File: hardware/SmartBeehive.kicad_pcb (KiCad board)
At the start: 4 copper layers, 7 parts, among them U1 ESP32-S3-DevKitC, U2 HX711_Module, U3 SSD1306, U4 DS18B20, U5 INMP441, U6 SHT31

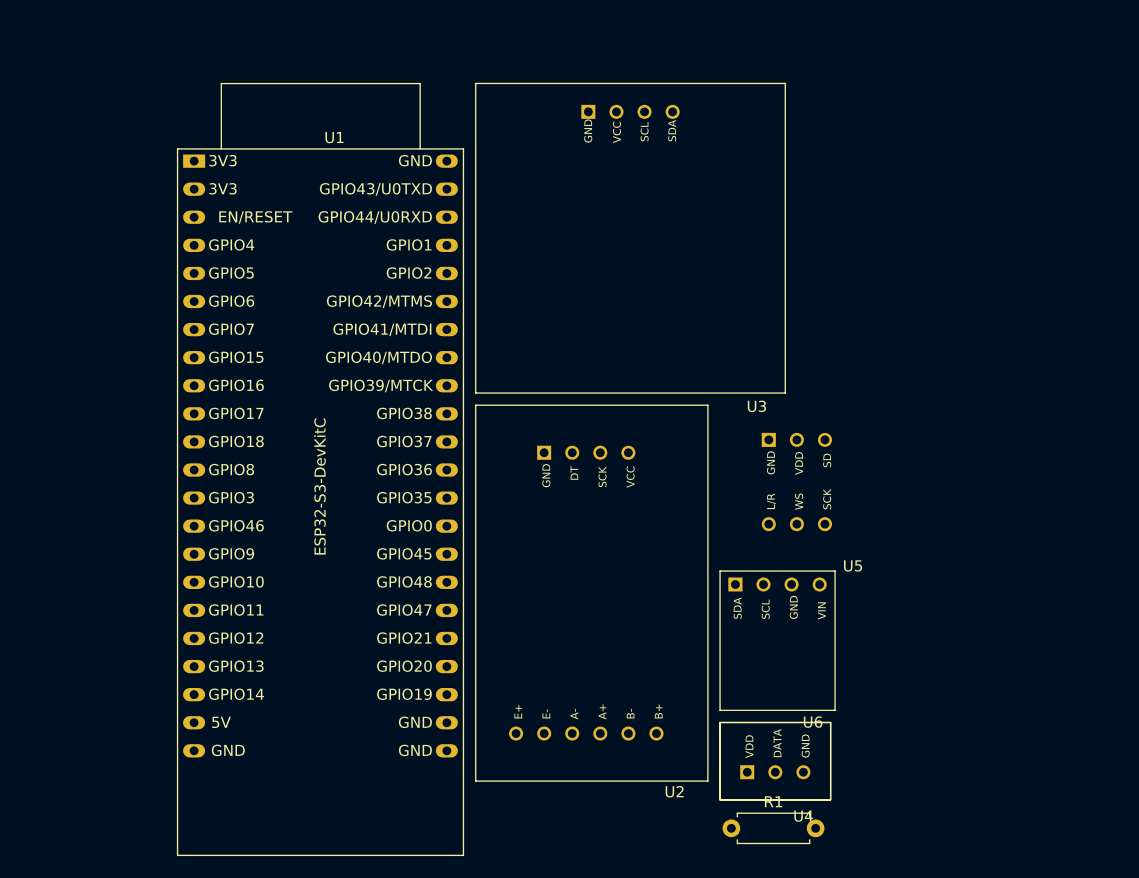
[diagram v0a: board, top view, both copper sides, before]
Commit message: Update component footprints and UUIDs in SmartBeehiveLib
- Modified the HX711_V2.kicad_mod file to update UUIDs and adjust text sizes for better visibility.
- Adjusted the INMP441.kicad_mod file, including repositioning text labels and updating UUIDs.
- Updated SHT31.kicad_mod with new UUIDs and repositioned several text labels for clarity.
- Revised SSD1306.kicad_mod to enhance text positioning and update UUIDs.
- Added lock files for the PCB, project, and schematic to track changes and prevent conflicts.
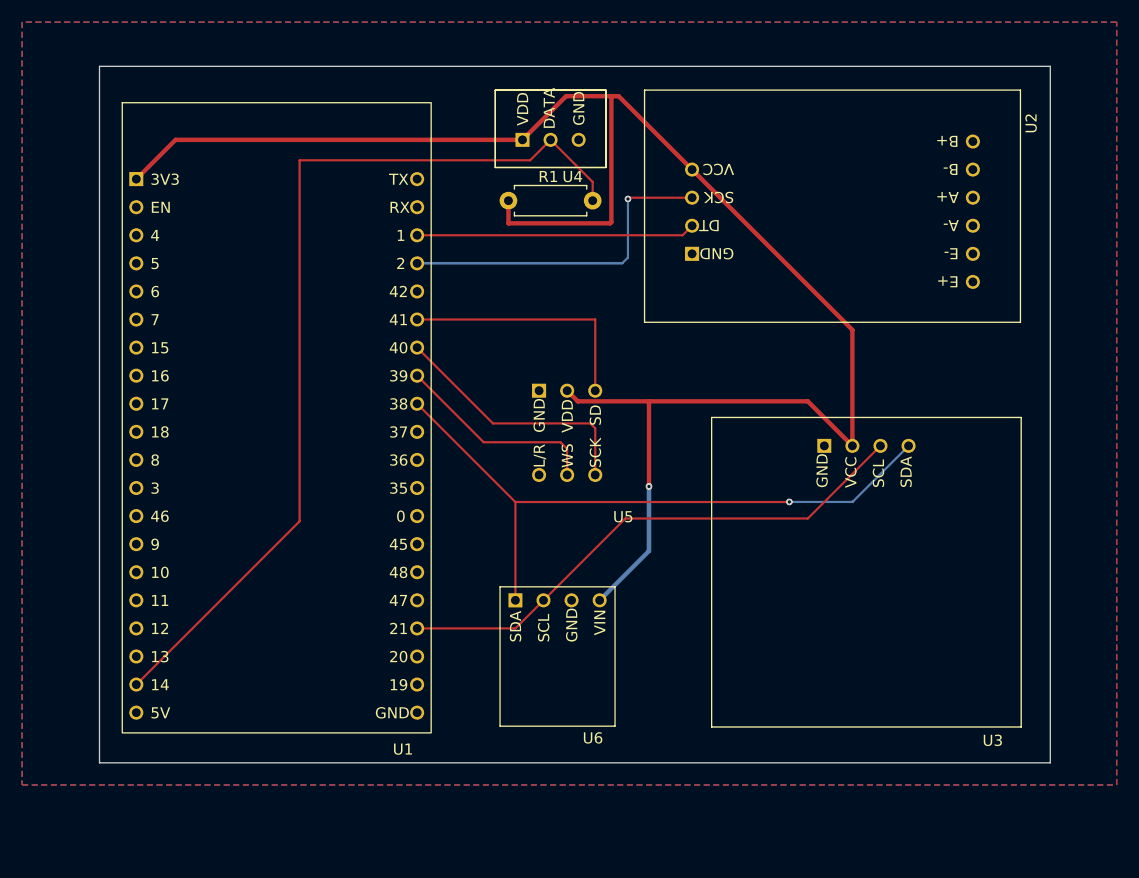
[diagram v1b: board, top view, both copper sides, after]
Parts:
- U1: value ESP32-S3-DevKitC -> ~; footprint PCM_Espressif:ESP32-S3-DevKitC -> SmartBeehiveLib:Freenove_ESP32_S3
- moved U4 60.7 mm to (137.8, 71.7)
- moved R1 60.2 mm to (134.0, 78.2)
- moved U2 41.1 mm to (163.3, 79.2), turned to 90 degrees
- moved U3 37.0 mm to (166.4, 111.8)
- moved U1 24.4 mm to (113.0, 97.8)
- moved U5 21.3 mm to (139.3, 99.2)
- moved U6 20.0 mm to (138.4, 119.4)
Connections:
- R1 pad 2: Net-(U1-GPIO14/ADC2_CH3) -> Net-(U1-GPIO14)
- U1 pad 19: unconnected-(U1-GPIO13/ADC2_CH2-Pad19) -> Net-(U1-GPIO14)
- U1 pad 2: +3V3 -> unconnected-(U1-EN-Pad2)
- U1 pad 20: Net-(U1-GPIO14/ADC2_CH3) -> unconnected-(U1-5V-Pad20)
- U1 pad 22: GND -> unconnected-(U1-GPIO44-Pad22)
- U1 pad 23: GND -> Net-(U1-GPIO1)
- U1 pad 24: GND -> Net-(U1-GPIO2)
- U1 pad 26: unconnected-(U1-GPIO20/USB_D+-Pad26) -> Net-(U1-GPIO41)
- U1 pad 27: Net-(U1-GPIO21) -> Net-(U1-GPIO40)
- U1 pad 28: unconnected-(U1-GPIO47-Pad28) -> Net-(U1-GPIO39)
- U1 pad 29: unconnected-(U1-GPIO48-Pad29) -> Net-(U1-GPIO38)
- U1 pad 35: Net-(U1-GPIO38) -> unconnected-(U1-GPIO48-Pad35)
- U1 pad 36: Net-(U1-GPIO39/MTCK) -> unconnected-(U1-GPIO47-Pad36)
- U1 pad 37: Net-(U1-GPIO40/MTDO) -> Net-(U1-GPIO21)
- U1 pad 38: Net-(U1-GPIO41/MTDI) -> unconnected-(U1-GPIO20-Pad38)
- U1 pad 40: Net-(U1-GPIO2/ADC1_CH1) -> GND
- U2 pad 2: Net-(U1-GPIO1/ADC1_CH0) -> Net-(U1-GPIO1)
- U2 pad 3: Net-(U1-GPIO2/ADC1_CH1) -> Net-(U1-GPIO2)
- U4 pad 2: Net-(U1-GPIO14/ADC2_CH3) -> Net-(U1-GPIO14)
- U5 pad 3: Net-(U1-GPIO41/MTDI) -> Net-(U1-GPIO41)
- U5 pad 5: Net-(U1-GPIO39/MTCK) -> Net-(U1-GPIO39)
- U5 pad 6: Net-(U1-GPIO40/MTDO) -> Net-(U1-GPIO40)
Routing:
- net +3V3: track 0.00 -> 157.7 mm, vias 0 -> 1
- net Net-(U1-GPIO14): track 0.00 -> 84.1 mm
- net Net-(U1-GPIO38): track 0.00 -> 59.1 mm, vias 0 -> 1
- net Net-(U1-GPIO21): track 0.00 -> 48.7 mm
- net Net-(U1-GPIO2): track 0.00 -> 30.4 mm, vias 0 -> 1
- net Net-(U1-GPIO1): track 0.00 -> 25.2 mm
- net Net-(U1-GPIO40): track 0.00 -> 23.4 mm
- net Net-(U1-GPIO41): track 0.00 -> 22.5 mm
- net Net-(U1-GPIO39): track 0.00 -> 18.7 mm
- added copper zone on B.Cu, net GND
- added copper zone on F.Cu, net GND
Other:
- board outline added: 86 x 63 mm

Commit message: Remove lock files for KiCad PCB, Pro, and Schematic to prevent conflicts during collaborative development.
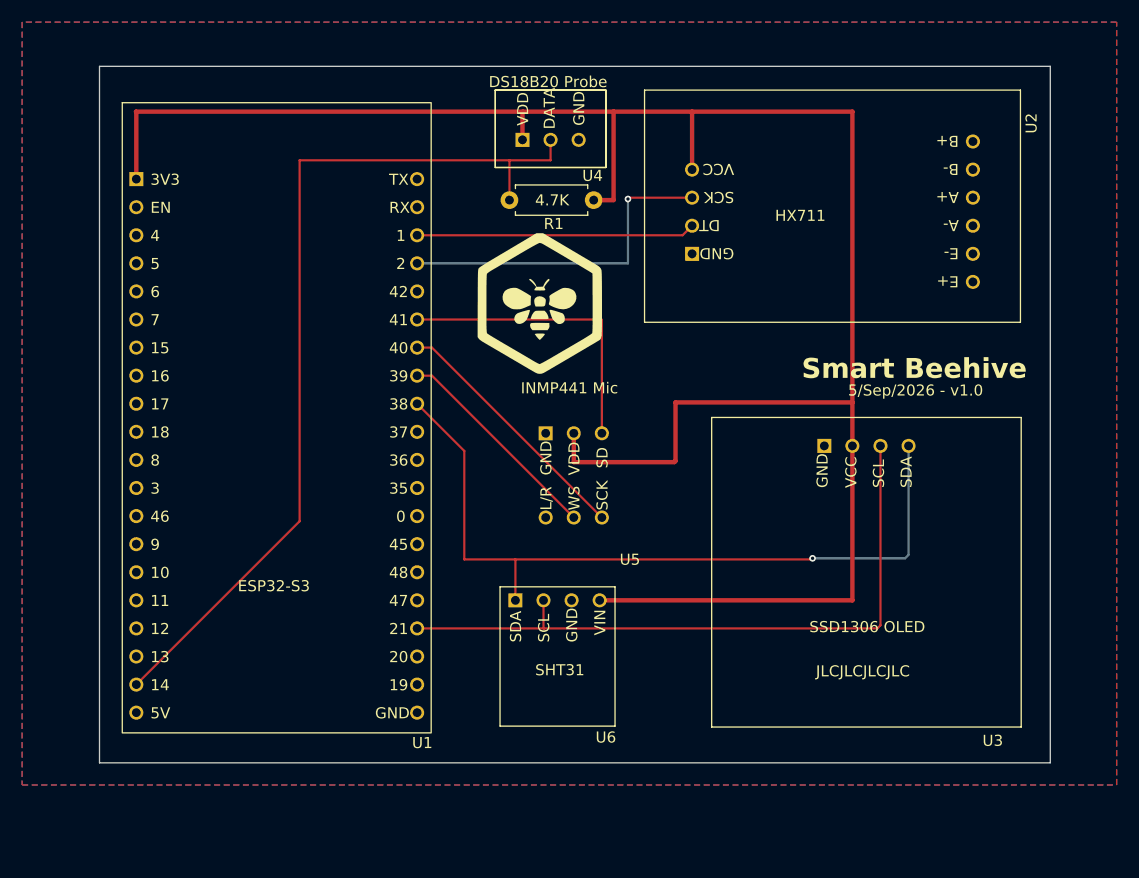
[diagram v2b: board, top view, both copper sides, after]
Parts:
- added G***: LOGO, LOGO, F.Cu at (136.7, 87.6)
- moved R1 7.71 mm to (141.7, 78.1), turned to 180 degrees
- moved U5 3.90 mm to (139.9, 103.0)
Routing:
- net +3V3: track 157.7 -> 188.7 mm, vias 1 -> 0
- net Net-(U1-GPIO21): track 48.7 -> 60.8 mm
- net Net-(U1-GPIO38): track 59.1 -> 69.8 mm
- net Net-(U1-GPIO41): track 22.5 -> 27.0 mm
- net Net-(U1-GPIO14): track 84.1 -> 81.7 mm
- net Net-(U1-GPIO39): track 18.7 -> 19.5 mm
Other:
- board text added: "4.7K"
- board text added: "5/Sep/2026 - v1.0"
- board text added: "DS18B20 Probe"
- board text added: "ESP32-S3"
- board text added: "HX711"
- board text added: "INMP441 Mic"
- board text added: "JLCJLCJLCJLC"
- board text added: "SHT31"
- board text added: "SSD1306 OLED"
- board text added: "Smart Beehive"

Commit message: Add lock file for SmartBeehive project to track user session
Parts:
- added P1: MountingHole_2.2mm_M2, MountingHole:MountingHole_2.2mm_M2, F.Cu at (110.0, 75.9)
- added P2: MountingHole_2.2mm_M2, MountingHole:MountingHole_2.2mm_M2, F.Cu at (110.0, 120.0)
- added P3: MountingHole_2.2mm_M2, MountingHole:MountingHole_2.2mm_M2, F.Cu at (175.0, 120.0)
- added P4: MountingHole_2.2mm_M2, MountingHole:MountingHole_2.2mm_M2, F.Cu at (160.0, 75.9)
